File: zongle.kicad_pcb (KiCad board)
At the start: 6 copper layers, 13.5 x 14.4 mm, 20 parts, among them U1 453-00059R

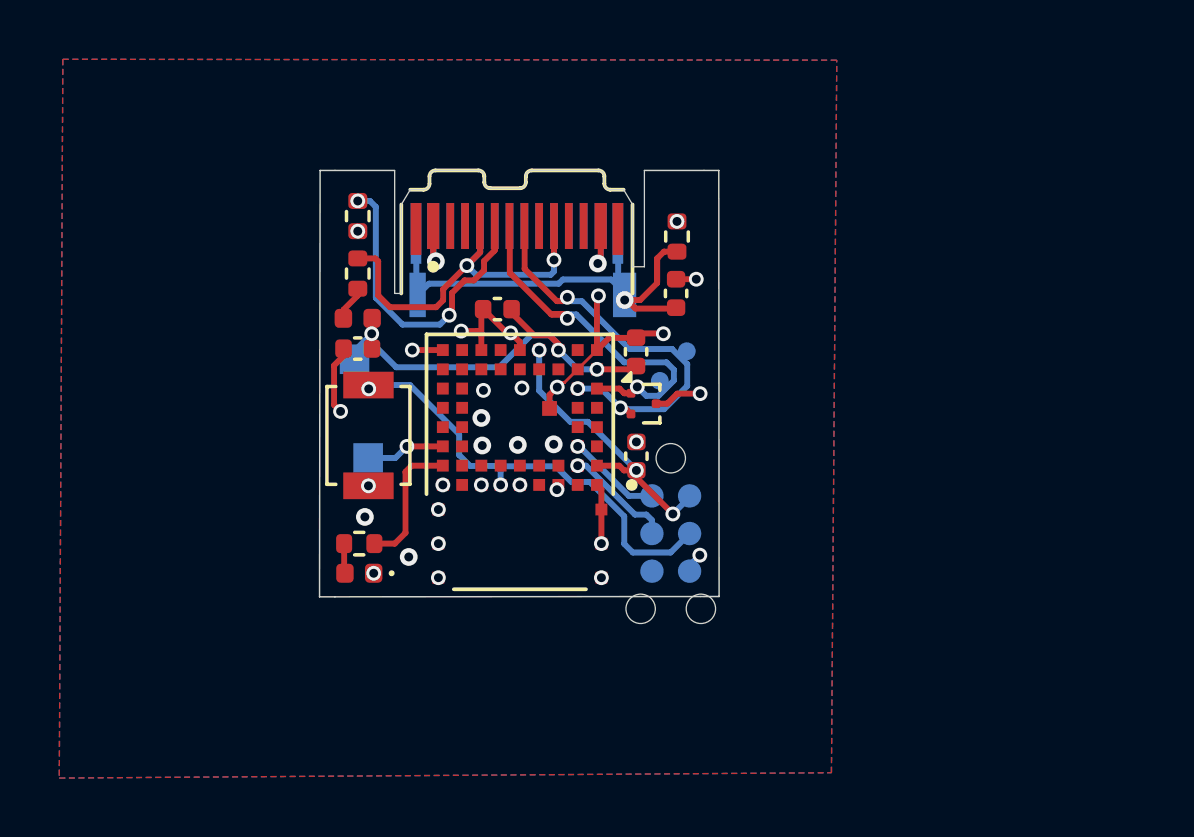
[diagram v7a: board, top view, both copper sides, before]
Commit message: some tweaks to usb routing. move power cap closer to vdd
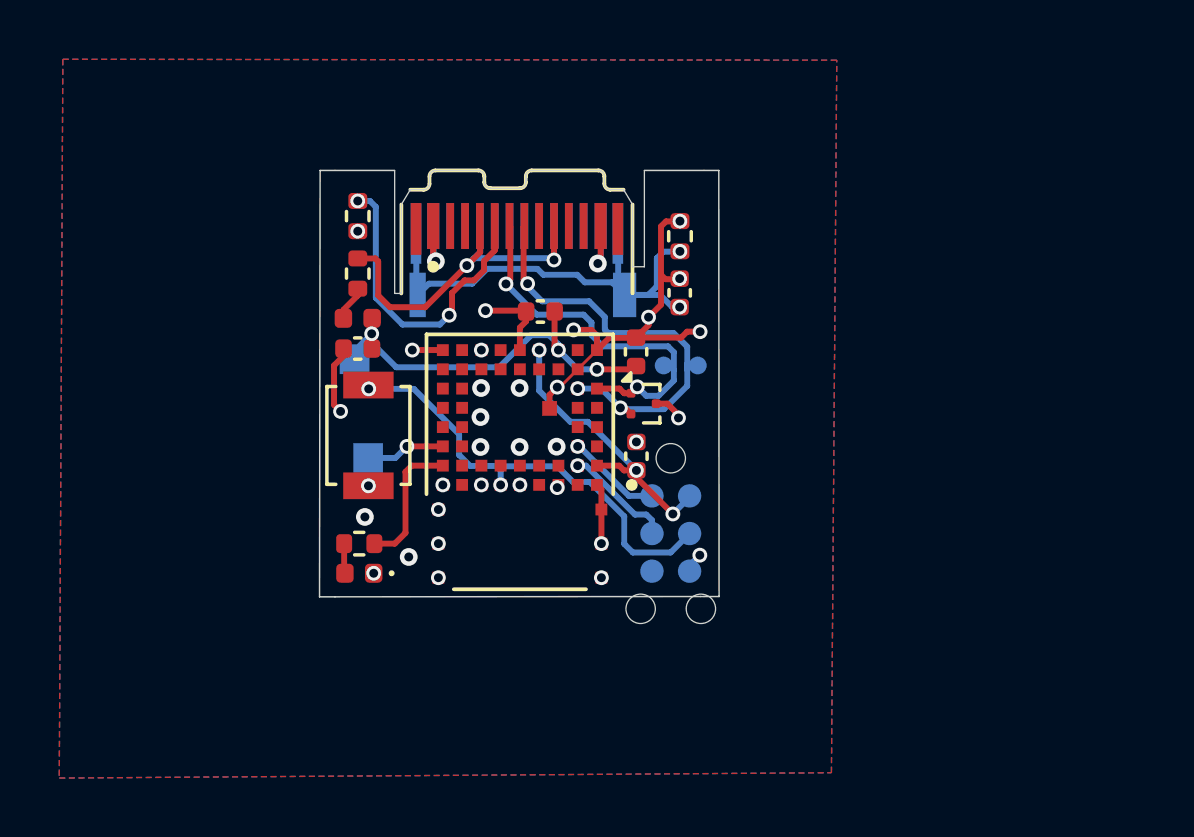
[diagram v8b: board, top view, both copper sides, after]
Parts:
- moved C23 1.45 mm to (152.5, 107.3)
- moved TpD- 0.61 mm to (157.8, 109.1)
- moved TpD+ 0.54 mm to (156.6, 109.1)
- moved C26 0.12 mm to (157.2, 106.7)
- moved R26 0.10 mm to (157.2, 104.7)
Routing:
- net GND: track 27.3 -> 33.0 mm, vias 35 -> 36
- net D-: track 14.1 -> 14.8 mm
- net VBUS_Raw: track 14.3 -> 13.7 mm
- net +5V: track 14.6 -> 14.0 mm
- net D+: track 12.4 -> 12.9 mm
- net Net-(C26-Pad1): track 16.7 -> 16.9 mm, vias 1 -> 2
